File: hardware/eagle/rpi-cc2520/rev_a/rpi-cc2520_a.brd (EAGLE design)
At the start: 19.6 x 34 mm, 22 parts, among them P1 MOLEX_73251-135X, U1 CC2520, X1 NX2520SA

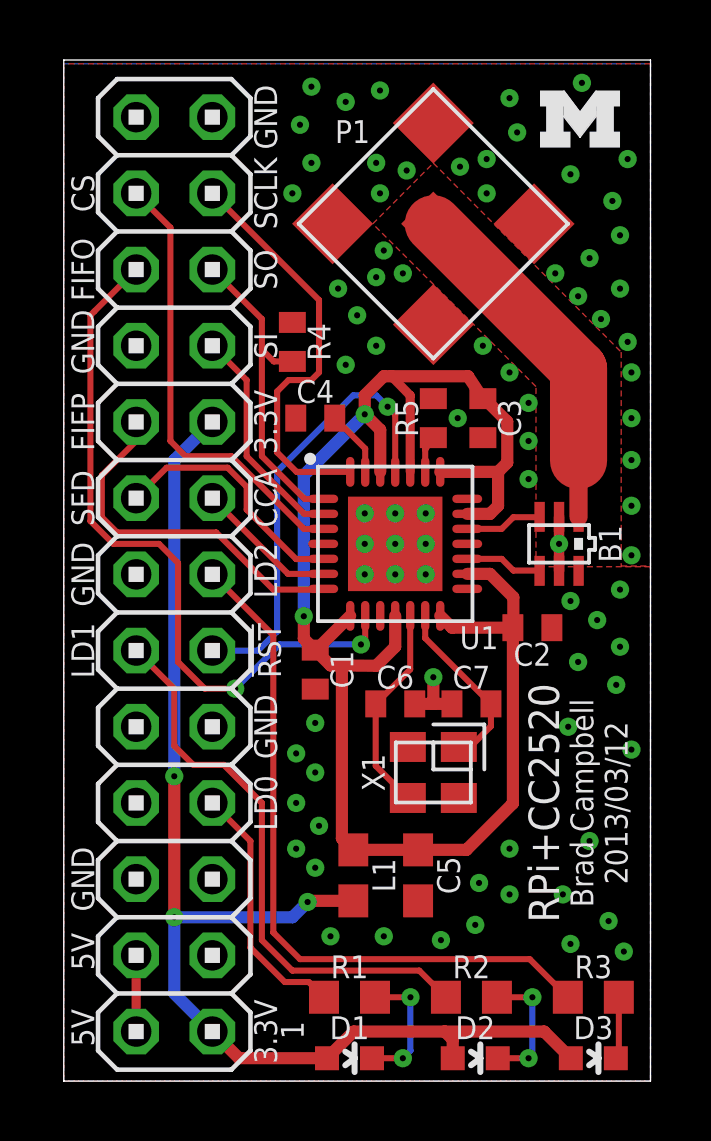
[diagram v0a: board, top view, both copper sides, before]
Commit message: Added ID chip to board.
This is important for creating a mac address. Otherwise the 15.4 side
doesn't have a good way of getting a unique address.
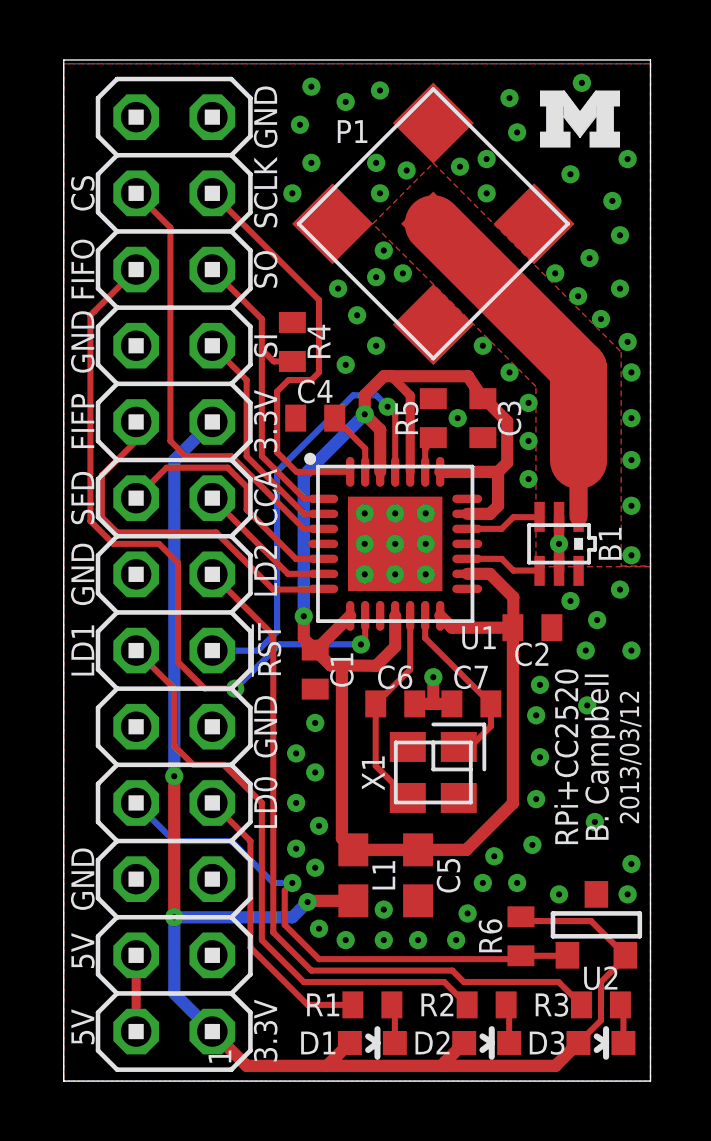
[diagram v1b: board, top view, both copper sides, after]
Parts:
- added R6: 2.2k, rcl:R0402
- added U2: DS2411, chips:SOT-23
- R1, R2, R3: device rcl:R0603 -> rcl:R0402
- moved D1 0.92 mm to (10.3, 1.27)
- moved R1 0.80 mm to (10.3, 2.54)
- moved D2 0.64 mm to (14.1, 1.27)
- moved D3 0.57 mm to (17.9, 1.27)
- moved R2 0.57 mm to (14.1, 2.54)
- moved R3 0.36 mm to (17.9, 2.54)
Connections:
- removed net UART0_TXD: J1.8
- new net ID_DATA: J1.8, R6.1, U2.1
- net GND: now also U2.3
- net VCC: now also R6.2, U2.2
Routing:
- net ID_DATA: track 0.00 -> 17.8 mm, vias 0 -> 1
- net VCC: track 41.8 -> 50.4 mm
- net N$1: track 4.35 -> 1.31 mm, vias 2 -> 0
- net N$2: track 4.29 -> 1.31 mm, vias 2 -> 0
- net LED0: track 8.49 -> 9.56 mm
- net LED1: track 18.9 -> 19.7 mm
- net N$3: track 2.07 -> 1.31 mm
- net LED2: track 23.5 -> 24.1 mm
- net GND: vias 81 -> 86
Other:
- board text added: "B. Campbell"
- board text removed: "Brad Campbell"
